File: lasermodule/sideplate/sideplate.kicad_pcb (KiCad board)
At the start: 2 copper layers, 117 x 25.2 mm, 2 parts

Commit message: simplified loading in freecad, updated pcbs
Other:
- board text added: "PCB3D_BR_sideplate"
- board text added: "PCB3D_TL_sideplate"
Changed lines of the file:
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@@
     (effects (font (size 1 1) (thickness 0.15)))
+  )
+  (gr_text "PCB3D_TL_sideplate" (at 95.6945 91.2495) (layer "Cmts.User")
+    (effects (font (size 1 1) (thickness 0.15)) (justify left bottom))
+  )
+  (gr_text "PCB3D_BR_sideplate" (at 197.2945 119.1895) (layer "Cmts.User")
+    (effects (font (size 1 1) (thickness 0.15)) (justify left bottom))
   )
   (via (at 144.4645 100.2745) (size 0.8) (drill 0.4) (layers "F.Cu" "B.Cu") (free) (net 0))

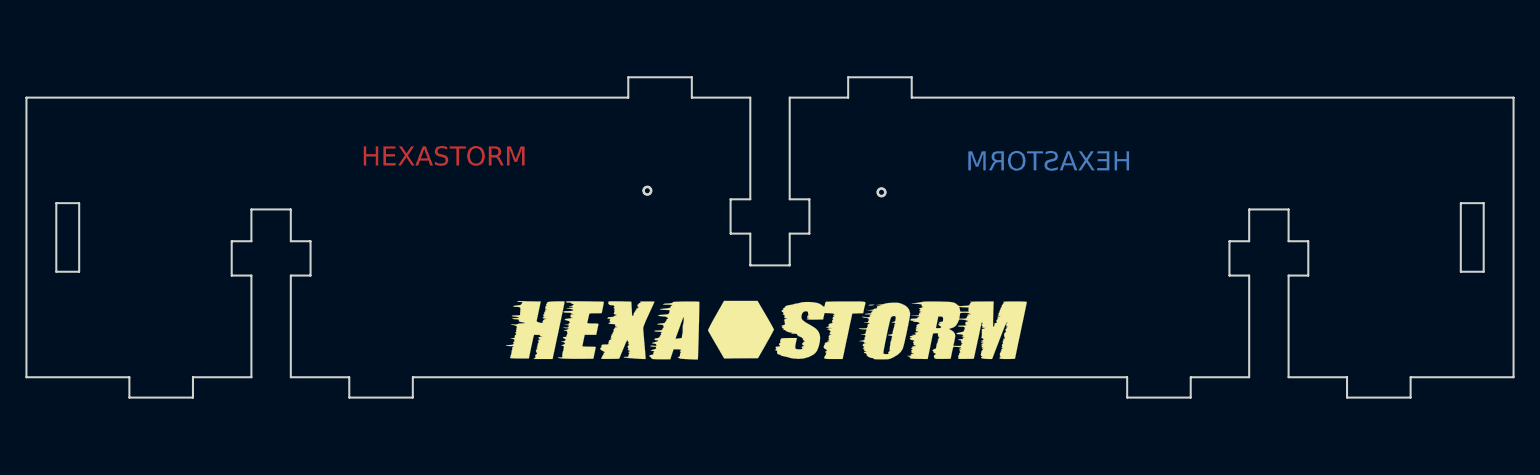
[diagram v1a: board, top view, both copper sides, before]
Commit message: pcbs can be rendered
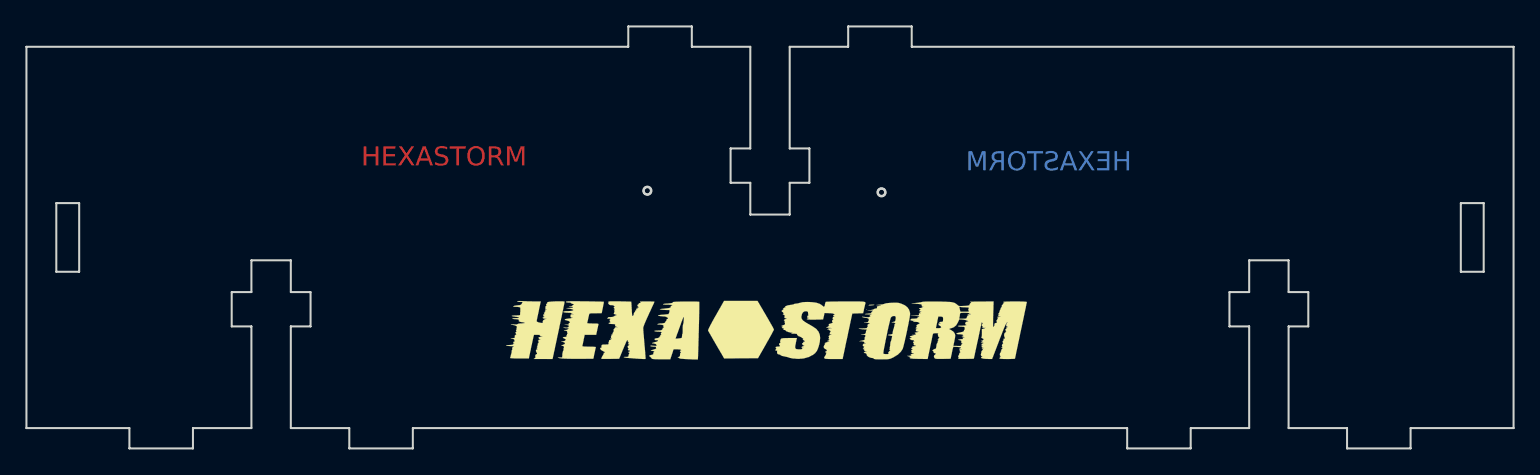
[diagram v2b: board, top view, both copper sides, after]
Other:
- board size 117 x 25.2 mm -> 117 x 33.2 mm

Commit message: changed position logos
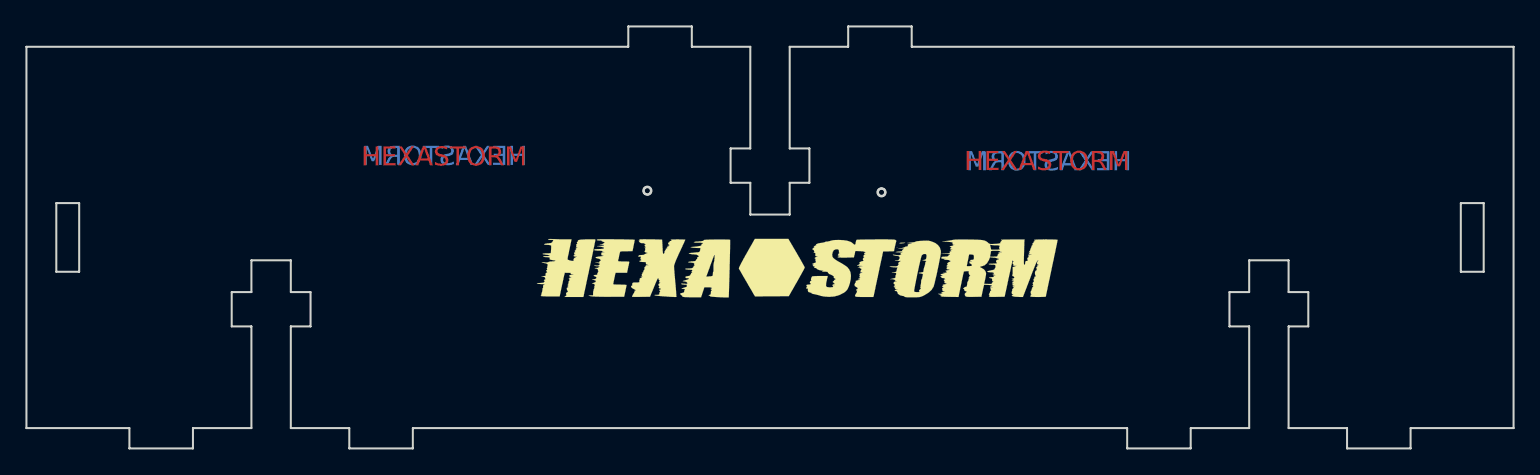
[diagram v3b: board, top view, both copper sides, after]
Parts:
- moved L1 5.45 mm to (156.2, 106.3)
- moved L2 5.34 mm to (152.2, 106.3)
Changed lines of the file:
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@@
   (net 0 "")
   (footprint "footprints:hexastorm" (layer "F.Cu")
-    (at 153.7903 111.2295)
+    (at 156.2145 106.3495)
     (property "Sheetfile" "sideplate.kicad_sch")
     (property "Sheetname" "")
@@
   )
   (footprint "footprints:hexastorm" (layer "B.Cu")
-    (at 154.3745 111.2295 180)
+    (at 152.2145 106.3495 180)
     (property "Sheetfile" "sideplate.kicad_sch")
     (property "Sheetname" "")
@@
   (gr_line (start 165.2645 87.3495) (end 165.2645 88.9495)
     (stroke (width 0.16) (type solid)) (layer "Edge.Cuts"))
+  (gr_text "HEXASTORM" (at 175.9145 97.9495) (layer "F.Cu")
+    (effects (font (size 1.5 1.5) (thickness 0.3)))
+  )
   (gr_text "HEXASTORM" (at 128.4745 97.5895) (layer "F.Cu")
     (effects (font (size 1.5 1.5) (thickness 0.3)))
   )
+  (gr_text "HEXASTORM\n" (at 128.5145 97.5495) (layer "B.Cu")
+    (effects (font (size 1.5 1.5) (thickness 0.3)) (justify mirror))
+  )
   (gr_text "HEXASTORM\n" (at 176.0395 97.9745) (layer "B.Cu")
     (effects (font (size 1.5 1.5) (thickness 0.3)) (justify mirror))
   )
-  (gr_text "HEXASTORM" (at 166.0145 103.4745) (layer "B.Mask")
+  (gr_text "HEXASTORM" (at 154.2145 115.2495) (layer "B.Mask")
     (effects (font (size 1 1) (thickness 0.15)) (justify mirror))
   )
-  (gr_text "HEXASTORM" (at 142.5395 103.1995) (layer "F.Mask")
+  (gr_text "HEXASTORM" (at 154.2145 115.2495) (layer "F.Mask")
     (effects (font (size 1 1) (thickness 0.15)))
   )
